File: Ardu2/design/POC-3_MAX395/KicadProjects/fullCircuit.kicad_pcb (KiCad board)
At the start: 2 copper layers, 189.2 x 143.5 mm, 127 parts, among them P1 CONN_01X02, P7 CONN_01X15, U1 Pyboard, U10 MAX395, U11 MAX395, U12 MAX395, U13 MAX395, U14 MAX395, U15 MAX395, U16 MAX395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

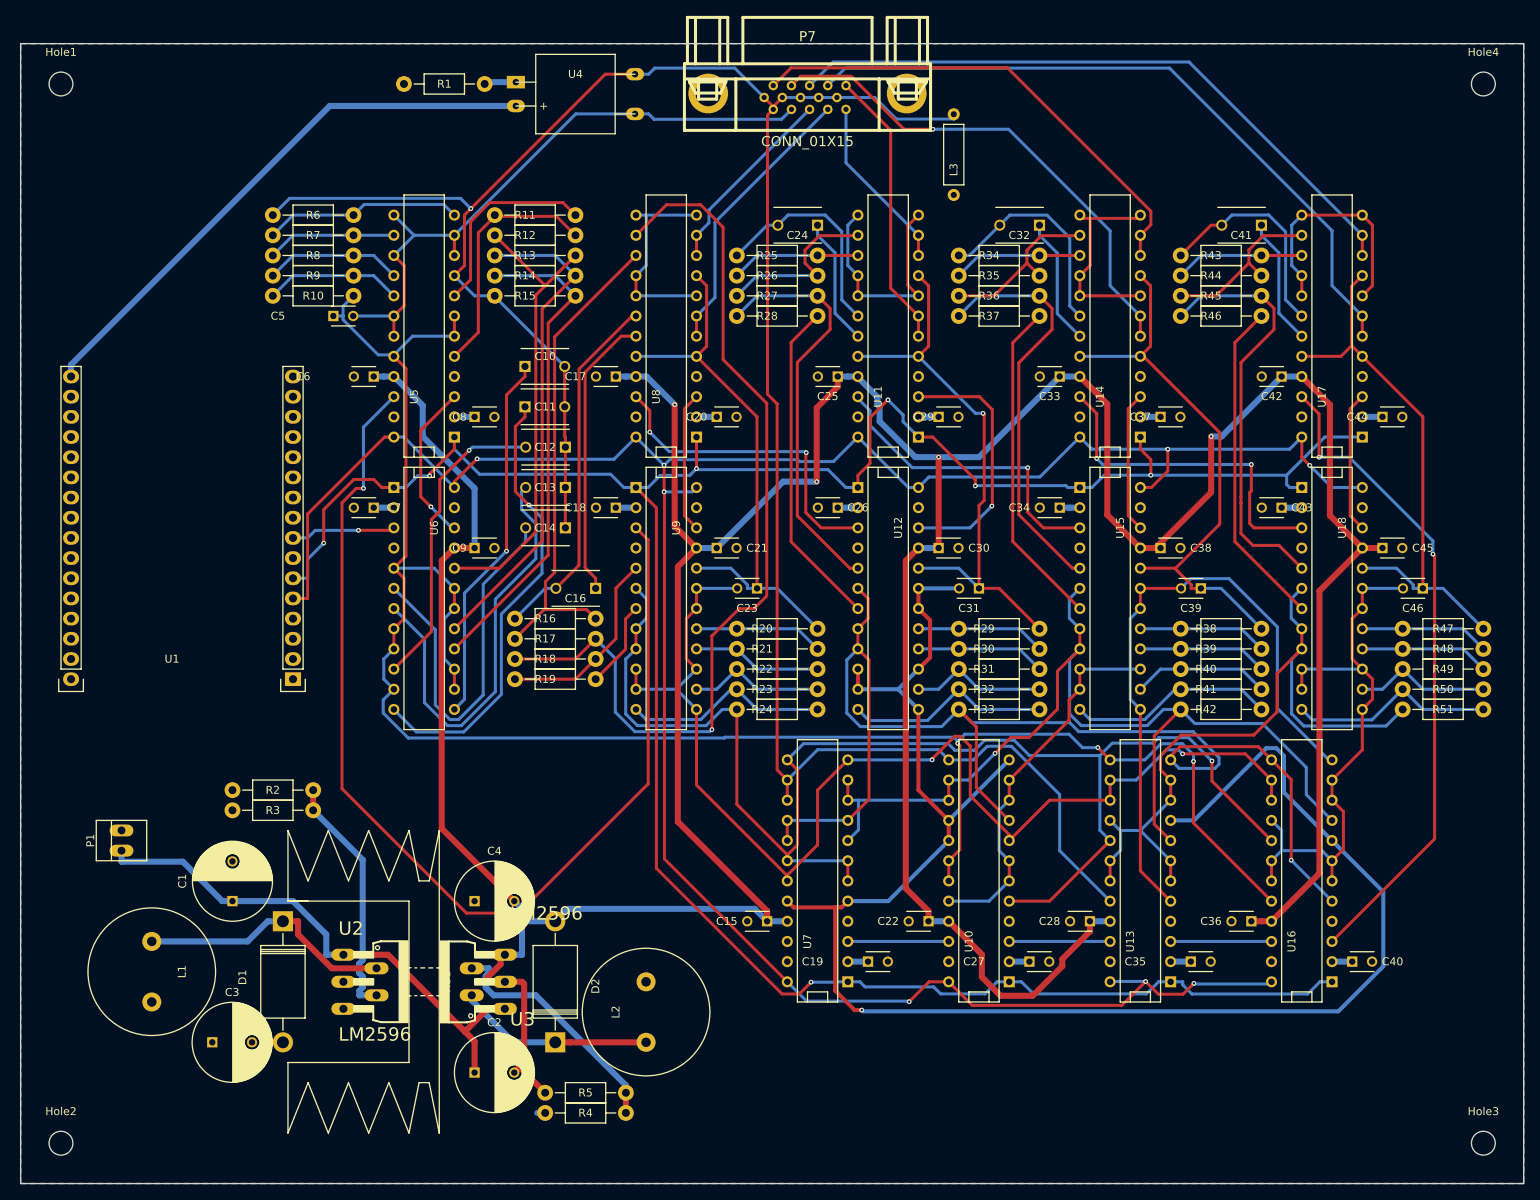
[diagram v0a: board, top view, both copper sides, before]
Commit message: updates after testing on breadboard - still need reverse polarity protection
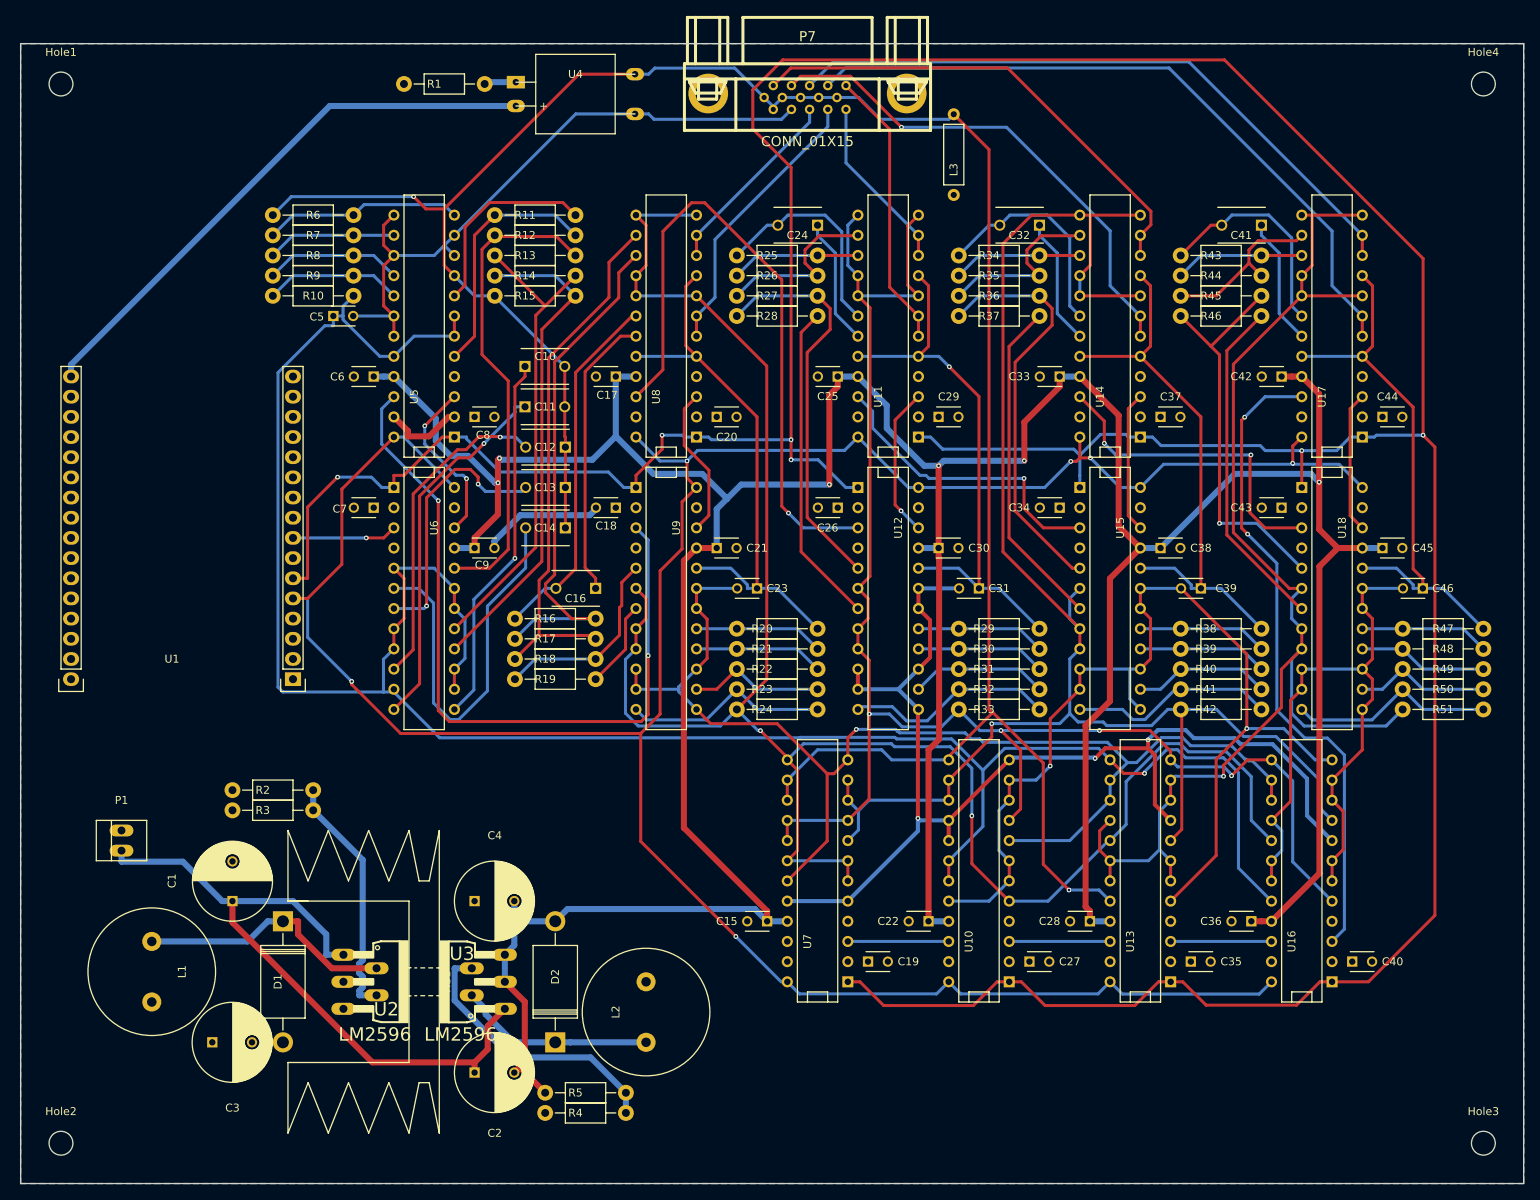
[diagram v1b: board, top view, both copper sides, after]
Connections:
- U11 pad 12: Net-(U11-Pad12) -> /COut-
- U11 pad 13: Net-(U11-Pad12) -> /COut-
- U11 pad 16: Net-(U11-Pad12) -> /COut-
- U11 pad 17: Net-(U11-Pad12) -> /COut-
- U11 pad 8: Net-(U11-Pad12) -> /COut-
- U14 pad 12: Net-(U14-Pad12) -> /BOut-
- U14 pad 13: Net-(U14-Pad12) -> /BOut-
- U14 pad 16: Net-(U14-Pad12) -> /BOut-
- U14 pad 17: Net-(U14-Pad12) -> /BOut-
- U14 pad 8: Net-(U14-Pad12) -> /BOut-
- U17 pad 12: Net-(U17-Pad12) -> /AOut-
- U17 pad 13: Net-(U17-Pad12) -> /AOut-
- U17 pad 16: Net-(U17-Pad12) -> /AOut-
- U17 pad 17: Net-(U17-Pad12) -> /AOut-
- U17 pad 8: Net-(U17-Pad12) -> /AOut-
- U8 pad 12: Net-(U8-Pad12) -> /DOut-
- U8 pad 13: Net-(U8-Pad12) -> /DOut-
- U8 pad 16: Net-(U8-Pad12) -> /DOut-
- U8 pad 17: Net-(U8-Pad12) -> /DOut-
- U8 pad 8: Net-(U8-Pad12) -> /DOut-
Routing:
- net /CLK: track 328.1 -> 483.7 mm, vias 7 -> 6
- net /BOut-: track 128.0 -> 209.3 mm
- net /COut+: track 217.3 -> 145.7 mm, vias 1 -> 3
- net /DOut-: track 176.1 -> 246.4 mm, vias 1 -> 2
- net /AOut-: track 89.8 -> 160.0 mm, vias 0 -> 1
- net Net-(R17-Pad2): track 118.0 -> 67.0 mm, vias 1 -> 0
- net Net-(U5-Pad22): track 137.2 -> 94.6 mm, vias 1 -> 2
- net Net-(U12-Pad3): track 40.9 -> 81.9 mm, vias 2 -> 1
- net /COut-: track 161.2 -> 201.5 mm, vias 1 -> 4
- net /MIn+: track 243.0 -> 278.4 mm, vias 3 -> 1
- net Net-(U11-Pad12): track 30.1 -> 0.00 mm
- net Net-(U17-Pad12): track 30.0 -> 0.00 mm
- net Net-(U8-Pad12): track 25.9 -> 0.00 mm
- net Net-(U14-Pad12): track 25.9 -> 0.00 mm
- net /V+: track 35.9 -> 10.1 mm
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
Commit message: reverse polarity added, Cout+ net corrected
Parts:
- added D3: 1N5401, Diodes_ThroughHole:Diode_DO-201AD_Horizontal_RM15, F.Cu at (82.5, 104.8)
- added F1: FUSE, Fuse_Holders_and_Fuses:Fuse_TE5_Littlefuse-395Series, F.Cu at (82.5, 113.0)
- moved P1 3.86 mm to (75.6, 114.3)
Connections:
- P1 pad 1: /BATin -> Net-(F1-Pad2)
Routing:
- net Net-(F1-Pad2): track 0.00 -> 6.97 mm
- net /BATin: track 85.8 -> 92.3 mm

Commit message: minor improvements to PCB
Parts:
- removed L3: 1mH, 330L:Inductor
- R1: value 220 -> 1K
- turned C15 to 90 degrees
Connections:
- C10 pad 2: /MIn- -> GND
- C11 pad 2: /MIn- -> GND
- C12 pad 1: /MIn- -> GND
- C13 pad 1: /MIn- -> GND
- C14 pad 1: /MIn- -> GND
- P7 pad 1: /MIn- -> GND
- P7 pad 10: /MIn- -> GND
- P7 pad 6: /MIn- -> GND
- P7 pad 7: /MIn- -> GND
- P7 pad 8: /MIn- -> GND
- P7 pad 9: /MIn- -> GND
- R15 pad 1: /MIn- -> GND
- R6 pad 1: /MIn- -> GND
- U10 pad 13: /MIn- -> GND
- U13 pad 20: /MIn- -> GND
- U4 pad 3: /MIn- -> GND
- U5 pad 9: /MIn- -> GND
- U7 pad 14: /MIn- -> GND
- U7 pad 15: /MIn- -> GND
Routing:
- net /MIn-: track 289.5 -> 0.00 mm, vias 2 -> 0
- net GND: track 15.9 -> 118.0 mm, vias 0 -> 1
- net /V-: track 530.9 -> 529.8 mm
- net /CS: track 341.3 -> 340.8 mm, vias 6 -> 5

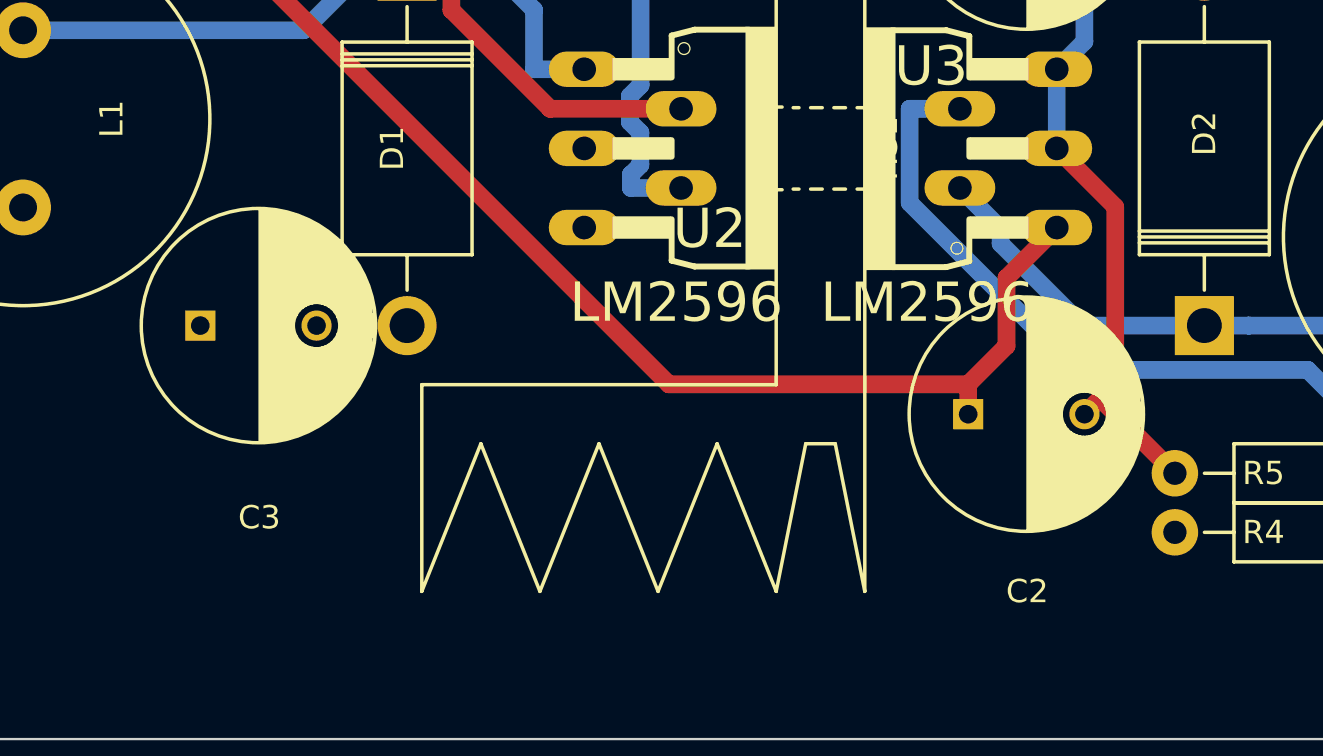
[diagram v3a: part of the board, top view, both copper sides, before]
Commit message: Updates after mockup of PCB
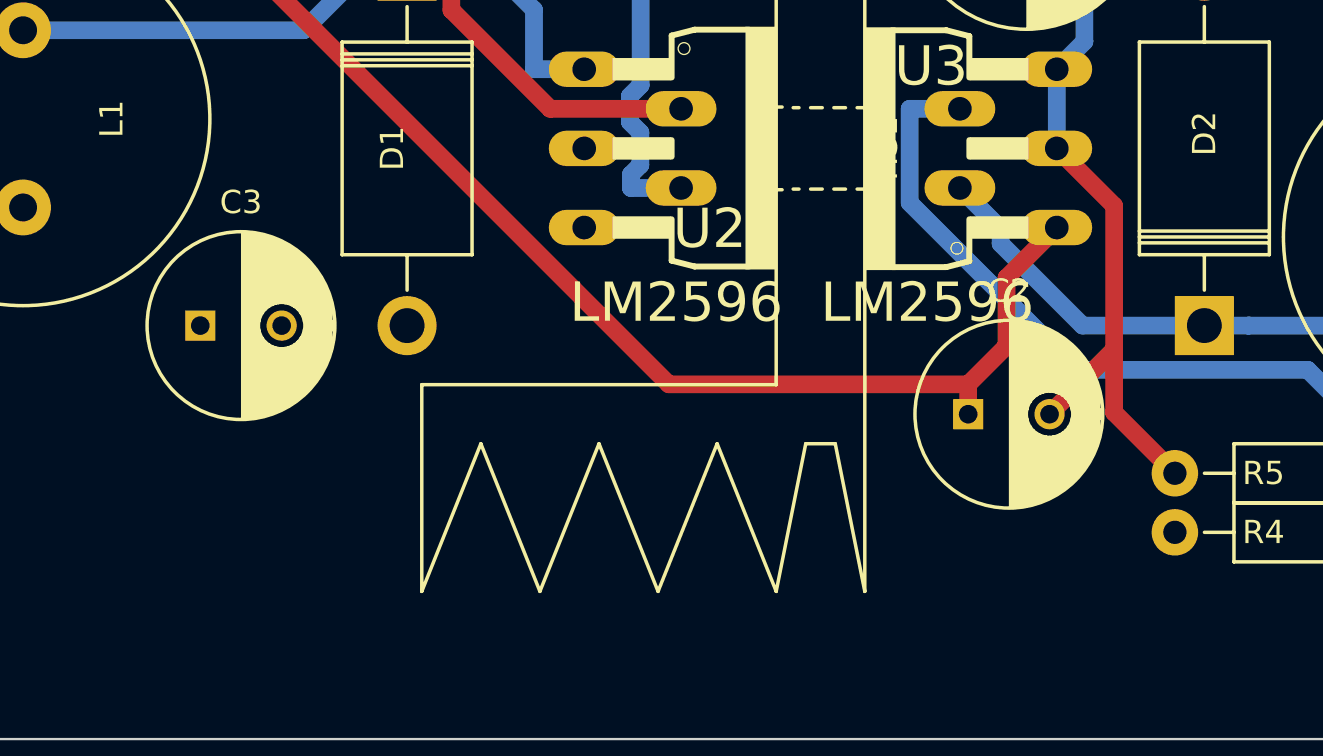
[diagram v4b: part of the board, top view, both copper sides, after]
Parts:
- C2, C3: footprint Capacitors_ThroughHole:C_Radial_D10_L16_P5 -> Capacitors_ThroughHole:C_Radial_D8_L11.5_P3.5
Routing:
- net /V-: track 529.8 -> 532.3 mm

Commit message: Preparing GERBER generation
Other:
- board text added: "Ardu2 Bottom Layer"
- board text added: "Ardu2 Top Layer"
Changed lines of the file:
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@@
     (links 477)
     (no_connects 0)
-    (area 62.179999 17.729999 251.510001 161.340001)
+    (area 62.179999 13.652499 251.510001 161.340001)
     (thickness 1.6)
-    (drawings 10)
+    (drawings 12)
     (tracks 1201)
     (zones 0)
@@
     (pad_drill 0.6)
     (pad_to_mask_clearance 0)
-    (aux_axis_origin 0 0)
+    (aux_axis_origin 67.31 156.21)
     (visible_elements FFFFFFFF)
     (pcbplotparams
-      (layerselection 0x2bfaa_80000007)
-      (usegerberextensions false)
+      (layerselection 0x000aa_80000001)
+      (usegerberextensions true)
       (excludeedgelayer false)
       (linewidth 0.100000)
@@
       (padsonsilk true)
       (subtractmaskfromsilk false)
-      (outputformat 4)
+      (outputformat 1)
       (mirror false)
-      (drillshape 2)
+      (drillshape 0)
       (scaleselection 1)
       (outputdirectory /home/bob/ArduGuitar/Ardu2/design/POC-3_MAX395/KicadProjects/))
@@
     )
   )
+  (gr_text "Ardu2 Top Layer" (at 168.0464 147.574) (layer F.Cu_Audio.GND)
+    (effects (font (size 1.5 1.5) (thickness 0.3)))
+  )
+  (gr_text "Ardu2 Bottom Layer" (at 203.9874 147.447) (layer B.Cu_SPI.VMinus)
+    (effects (font (size 1.5 1.5) (thickness 0.3)) (justify mirror))
+  )
   (gr_line (start 248.92 17.78) (end 251.46 17.78) (angle 90) (layer Edge.Cuts) (width 0.1))
